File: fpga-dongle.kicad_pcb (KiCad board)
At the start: 2 copper layers, 85.8 x 137 mm, 82 parts, among them P1 right, P2 left, P3 CONN_01X20, U1 W25Q16BVSSIG(SOIC-8_208mil), U2 SY8009AAAC(SOT23-5), U3 SY8009AAAC(SOT23-5), U4 ICE40HX1K-VQ100(VQFP100), U5 AS4C16M16S

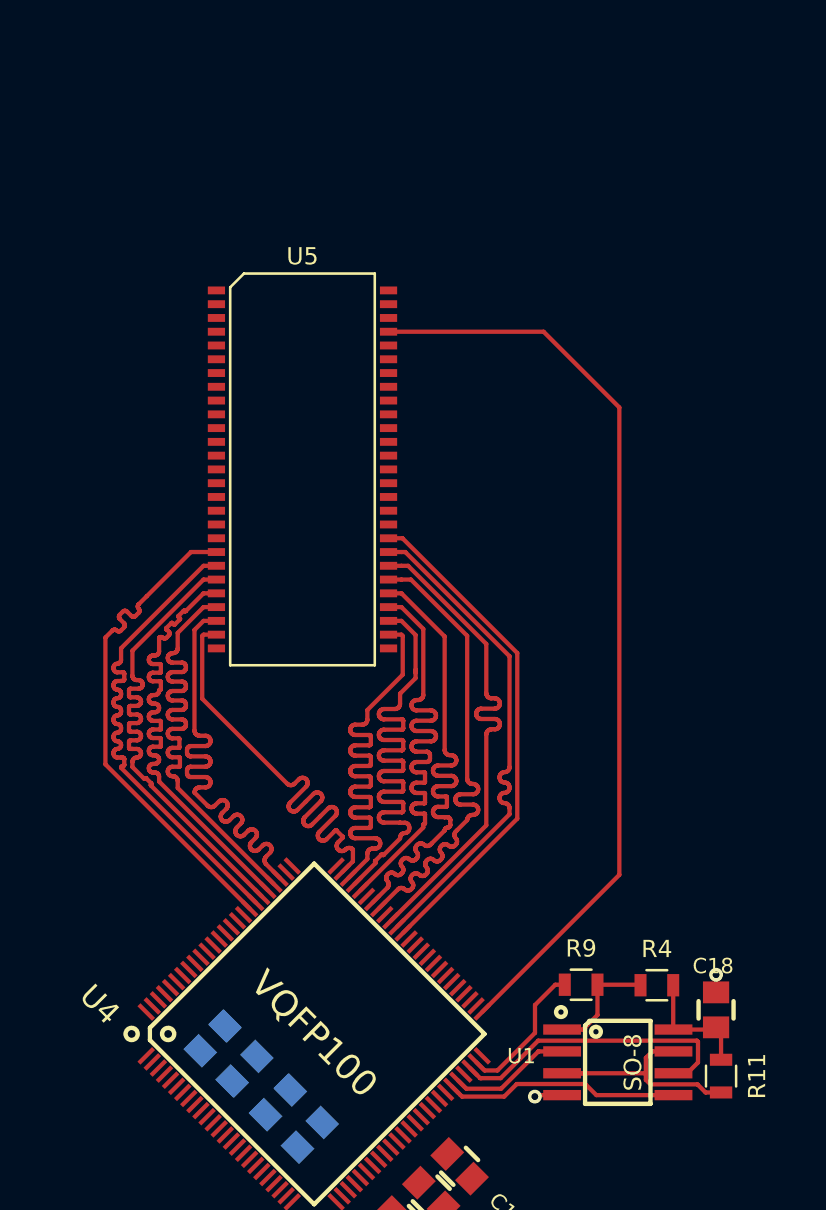
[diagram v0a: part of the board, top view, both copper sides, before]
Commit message: First 144LQFP version. To be revised
Signed-off-by: Martin Ribelotta <martinribelotta@gmail.com>
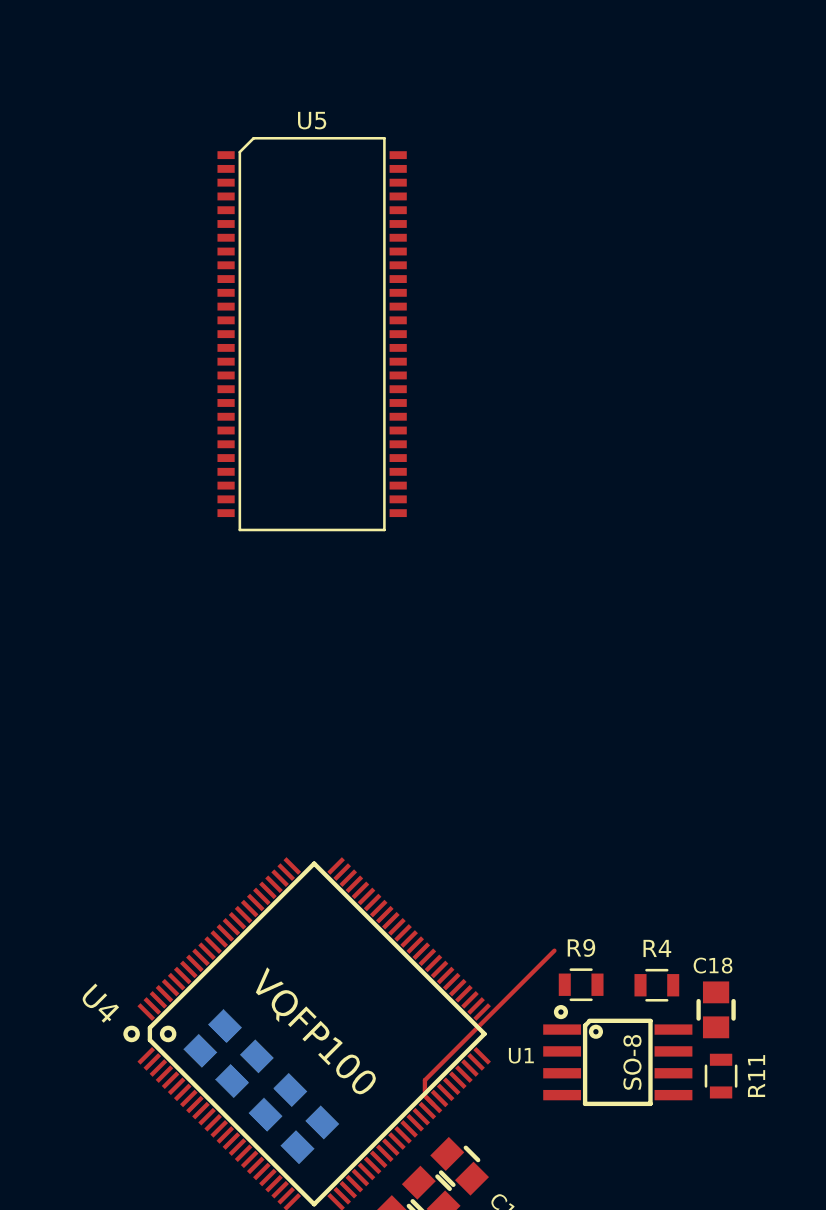
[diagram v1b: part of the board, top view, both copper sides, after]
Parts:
- moved U5 7.88 mm to (61.3, 69.4)
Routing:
- net /RAM_D14: track 53.7 -> 0.00 mm
- net /RAM_A6: track 33.4 -> 0.00 mm
- net /RAM_A2: track 29.3 -> 0.00 mm
- net /RAM_A15: track 29.3 -> 0.00 mm
- net /RAM_A4: track 29.3 -> 0.00 mm
- net /RAM_A8: track 29.3 -> 0.00 mm
- net /RAM_A7: track 29.3 -> 0.00 mm
- net /RAM_A3: track 29.3 -> 0.00 mm
- net /RAM_A12: track 29.3 -> 0.00 mm
- net /RAM_A9: track 29.3 -> 0.00 mm
- net /RAM_A1: track 29.3 -> 0.00 mm
- net /RAM_A10: track 29.3 -> 0.00 mm
- net /RAM_A11: track 29.3 -> 0.00 mm
- net /RAM_A13: track 29.3 -> 0.00 mm
- net /RAM_A5: track 29.2 -> 0.00 mm
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
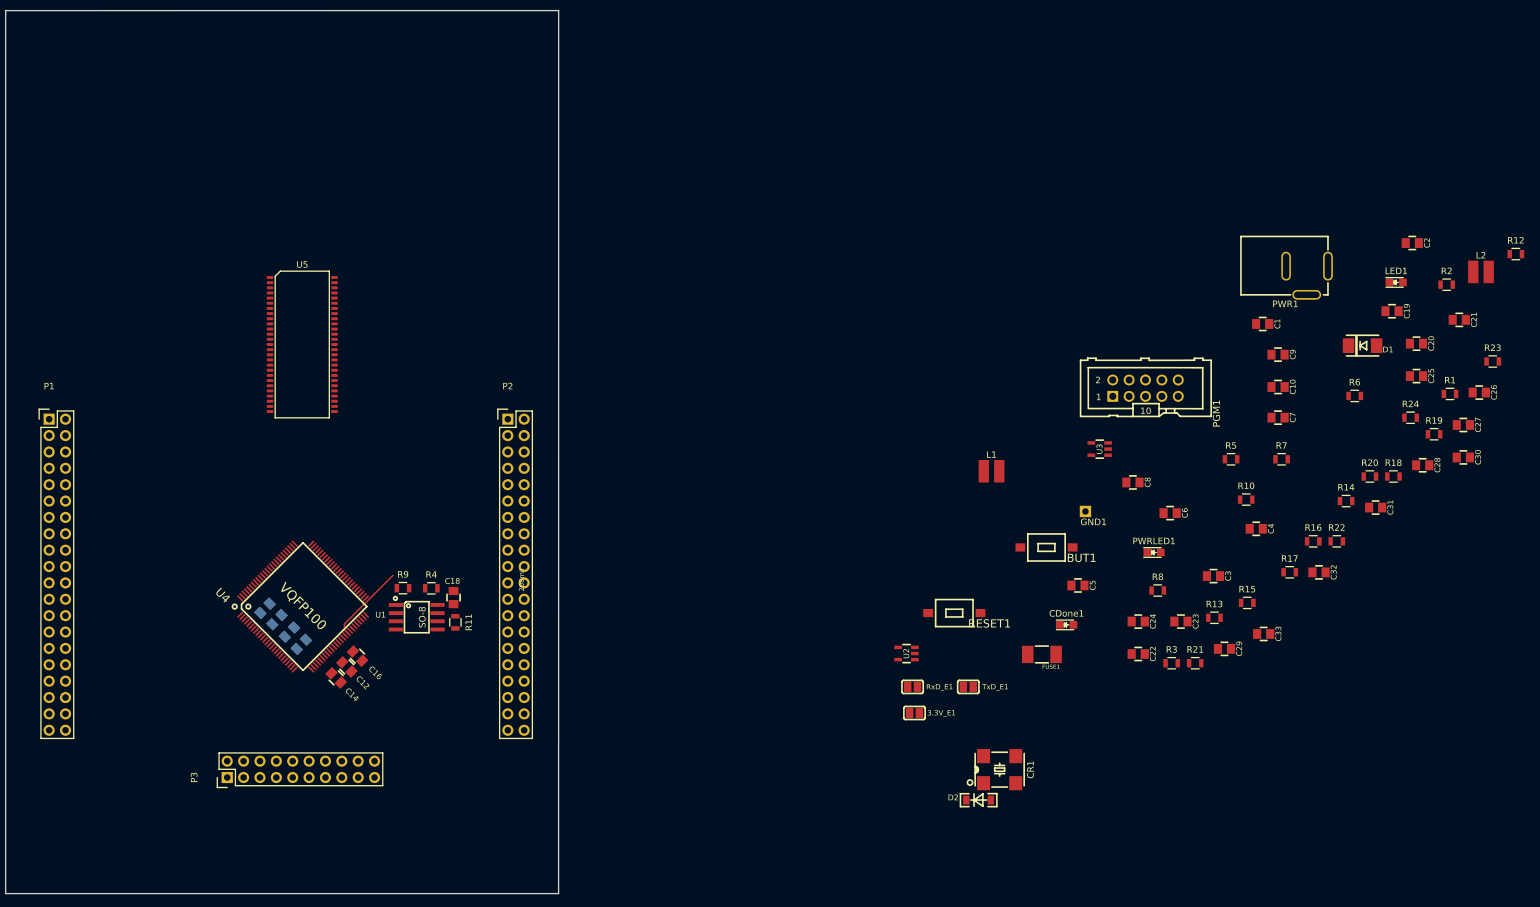
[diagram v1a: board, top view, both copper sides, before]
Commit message: First component assign and preeliminar place
Signed-off-by: Martin Ribelotta <martinribelotta@gmail.com>
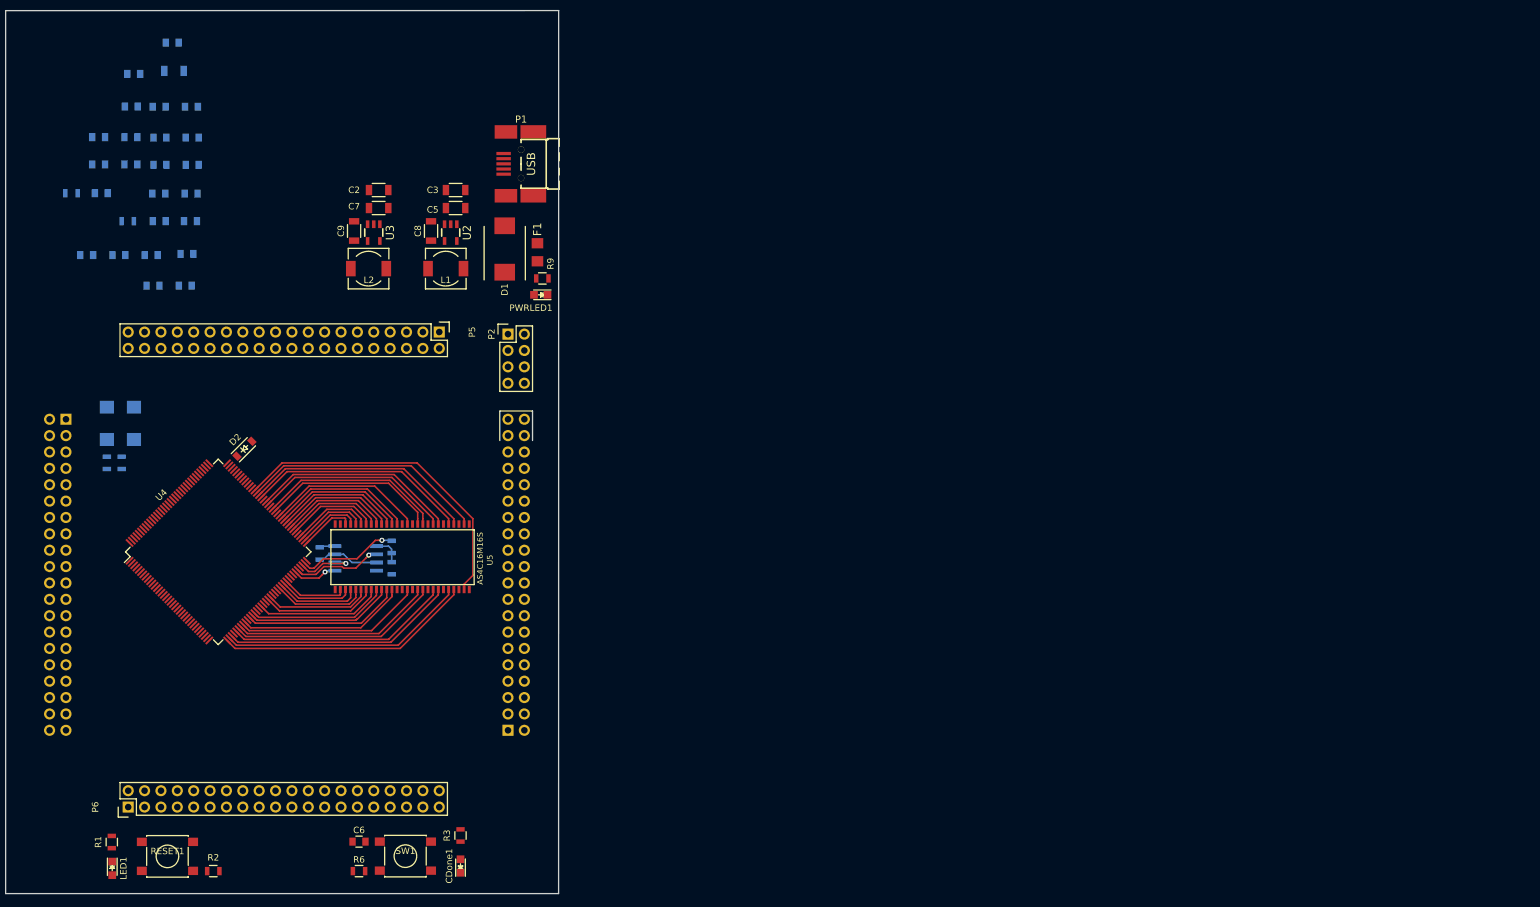
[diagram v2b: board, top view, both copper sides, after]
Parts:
- removed 3.3V_E1, RxD_E1, TxD_E1: Opened, OLIMEX:SJ
- removed BUT1: T1107A(6x3,8x2,5MM), OLIMEX:T1107A(6x3,8x2,5MM)
- removed C33: 100n, OLIMEX:C_0805_5MIL_DWS
- removed FUSE1: NA(5025), OLIMEX:FUSE-5025
- removed GND1: TESTPAD, OLIMEX:TEST_PAD40x70_SQUARE
- removed PGM1: BH10S, OLIMEX:UEXT_ML10
- removed PWR1: PWRJ-2mm(YDJ-1136), OLIMEX:PWRJ-2mm(YDJ-1136)
- removed R13: 22R, Resistors_SMD:R_0805
- removed R14, R15: 2.2k, Resistors_SMD:R_0805
- removed R16: 10k, Resistors_SMD:R_0805
- removed R17, R18, R19, R20, R21, R22, R23, R24: 0, Resistors_SMD:R_0805
- added F1: 1A, OLIMEX_Devices-FP:FUSE-1206, F.Cu at (97.8, 55.1)
- added P4: left, Pin_Headers:Pin_Header_Straight_2x20, B.Cu at (93.2, 129.3)
- added P5: CONN_01X40, Pin_Headers:Pin_Header_Straight_2x20, F.Cu at (82.6, 67.5)
- added P6: CONN_01X40, Pin_Headers:Pin_Header_Straight_2x20, F.Cu at (34.3, 141.2)
- added SW1: T1107A(6x3,8x2,5MM), Buttons_Switches_SMD:SW_SPST_PTS645, F.Cu at (77.3, 148.8)
- C1, C10: value 22uF/6.3V/0603 -> 100nF; footprint OLIMEX:C_0805_5MIL_DWS -> Capacitors_SMD:C_0805; moved to B.Cu
- C11: value 100nF -> 10uF; footprint OLIMEX:C_0805_5MIL_DWS -> Capacitors_SMD:C_1206
- C12, C14, C16, C18, C20, C21, C22, C23, C24, C25, C4: footprint OLIMEX:C_0805_5MIL_DWS -> Capacitors_SMD:C_0805; moved to B.Cu
- C13, C15, C17: footprint OLIMEX:C_0805_5MIL_DWS -> Capacitors_SMD:C_0805
- C19: value NA(100nF) -> 100nF; footprint OLIMEX:C_0805_5MIL_DWS -> Capacitors_SMD:C_0805; moved to B.Cu
- C2, C5: footprint OLIMEX:C_0805_5MIL_DWS -> Capacitors_SMD:C_1206
- C26: value 100p -> 100nF; footprint OLIMEX:C_0805_5MIL_DWS -> Capacitors_SMD:C_0805; moved to B.Cu
- C27, C28, C29, C30, C31, C32: value 100n -> 100nF; footprint OLIMEX:C_0805_5MIL_DWS -> Capacitors_SMD:C_0805; moved to B.Cu
- C3: value 100nF -> 22uF/6.3V/0603; footprint OLIMEX:C_0805_5MIL_DWS -> Capacitors_SMD:C_1206
- C6: value 47uF/6.3V/0805 -> NA(100nF); footprint OLIMEX:C_0805_5MIL_DWS -> Capacitors_SMD:C_0805
- C7: value 22uF/6.3V/0603 -> 47uF/6.3V/0805; footprint OLIMEX:C_0805_5MIL_DWS -> Capacitors_SMD:C_1206
- C8, C9: value 22uF/6.3V/0603 -> 10uF/6.3V/0603; footprint OLIMEX:C_0805_5MIL_DWS -> Capacitors_SMD:C_1206
- CR1: value Oscillator-100MHZ_TXC-7W -> Oscillator-50MHZ_TXC-7W; footprint OLIMEX:Oscillator_7.0x5.0mm -> OLIMEX_Crystal-FP:Oscillator_7.0x5.0mm; moved to B.Cu
- D1: footprint OLIMEX:DO214AA -> Diodes_SMD:DO-214AB
- D2: footprint OLIMEX:SOD-123_1C-2A_KA -> Diodes_SMD:SOD-123
- L1, L2: value 2.2uH/1.5A/DCR<0.1R/CD32 -> 2.2uH; footprint OLIMEX:CD32 -> Choke_SMD:Choke_SMD_6.3x6.3_H3
- P1: value right -> USB_PWR; footprint Pin_Headers:Pin_Header_Straight_2x20 -> OLIMEX_Connectors-FP:USB_Mini-B-NOSILK
- P2: value left -> PGM; footprint Pin_Headers:Pin_Header_Straight_2x20 -> Pin_Headers:Pin_Header_Straight_2x04
- P3: value CONN_01X20 -> right; footprint Pin_Headers:Pin_Header_Straight_2x10 -> Pin_Headers:Pin_Header_Straight_2x20; moved to B.Cu
- R1: value 10k -> 2.2k
- R10: value NA(22R) -> 22R; moved to B.Cu
- R11, R4: value 10k -> 22R; moved to B.Cu
- R12: value 22R -> 100R; moved to B.Cu
- R2: value 2.2k -> 10k
- R3, R9: value 22R -> 2.2k
- R5, R8: value 4.99k/1% -> 10k; moved to B.Cu
- R6: value 1.1k/1% -> 10k
- R7: value 4.99k/1% -> 22R; moved to B.Cu
- RESET1: footprint OLIMEX:T1107A(6x3,8x2,5MM) -> Buttons_Switches_SMD:SW_SPST_PTS645
- U1: footprint OLIMEX:SO-8_208mil -> OLIMEX_IC-FP:SOIC-8_208mil; moved to B.Cu
- U2: value SY8009AAAC(SOT23-5) -> sc189(Z) 3.3v; footprint OLIMEX:SOT-23-5 -> OLIMEX_Regulators-FP:SOT-23-5
- U3: value SY8009AAAC(SOT23-5) -> sc189(C) 1.2v; footprint OLIMEX:SOT-23-5 -> OLIMEX_Regulators-FP:SOT-23-5
- U4: value ICE40HX1K-VQ100(VQFP100) -> iCE40-HX4K-TQ144; footprint OLIMEX:VQFP100_Pitch-0.5mm_Dimensions-16.00x16.00x1.20mm -> Housings_QFP:LQFP-144_20x20mm_Pitch0.5mm
- U5: footprint OLIMEX:SOIC-54 -> mribelotta:TSOP_II_54
- moved R12 224.3 mm to (25.5, 46.0), turned to 180 degrees
- moved LED1 219.0 mm to (31.8, 150.7), turned to 270 degrees
- moved R1 219.0 mm to (31.8, 146.6), turned to 90 degrees
- moved C30 216.6 mm to (29.7, 41.5), turned to 180 degrees
- moved C26 213.8 mm to (34.8, 32.5), turned to 180 degrees
- moved R2 211.9 mm to (47.5, 151.1)
- moved C28 211.6 mm to (29.7, 37.3), turned to 180 degrees
- moved C21 203.6 mm to (39.2, 37.3), turned to 180 degrees
- moved C27 199.8 mm to (43.4, 55.4), turned to 180 degrees
- moved C25 197.7 mm to (39.2, 41.6), turned to 180 degrees
- moved C20 191.2 mm to (43.2, 60.3), turned to 180 degrees
- moved C31 190.1 mm to (44.1, 46.0), turned to 180 degrees
- moved C32 189.3 mm to (39.0, 46.0), turned to 180 degrees
- moved C19 188.1 mm to (44.2, 37.3), turned to 180 degrees
- moved C29 185.6 mm to (34.7, 41.5), turned to 180 degrees
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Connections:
- C1 pad 2: +5V -> +3V3
- C10 pad 1: GND -> /GNDPLL
- C10 pad 2: +1V2 -> /VCCPLL
- C11 pad 1: GND -> /GNDPLL
- C11 pad 2: +1V2 -> /VCCPLL
- C12 pad 1: GND -> +1V2
- C12 pad 2: +1V2 -> GND
- C13 pad 1: GND -> +1V2
- C13 pad 2: +3V3 -> GND
- C14 pad 1: GND -> +1V2
- C14 pad 2: +3V3 -> GND
- C15 pad 1: GND -> +1V2
- C15 pad 2: +3V3 -> GND
- C16 pad 1: GND -> +3V3
- C16 pad 2: +3V3 -> GND
- C17 pad 1: GND -> +3V3
- C17 pad 2: +3V3 -> GND
- C18 pad 1: GND -> +3V3
- C18 pad 2: +3V3 -> GND
- C19 pad 1: GND -> +3V3
- C19 pad 2: /BUT1 -> GND
- C20 pad 1: GND -> +3V3
- C20 pad 2: +3V3 -> GND
- C21 pad 1: GND -> +3V3
- C21 pad 2: +3V3 -> GND
- C22 pad 1: GND -> +3V3
- C22 pad 2: +3V3 -> GND
- C23 pad 1: GND -> +3V3
- C23 pad 2: +1V2 -> GND
- C24 pad 1: GND -> +3V3
- C24 pad 2: +3V3 -> GND
- C25 pad 1: GND -> +3V3
- C25 pad 2: +1V2 -> GND
- C3 pad 2: +3V3 -> +5V
- C6 pad 2: +5V -> /BUT1
- C7 pad 2: +3V3 -> +5V
- C8 pad 2: +1V2 -> +3V3
- C9 pad 2: +3V3 -> +1V2
- D2 pad 2: +3V3 -> +1V2
- L1 pad 1: +3V3 -> Net-(L1-Pad1)
- L1 pad 2: Net-(L1-Pad2) -> +3V3
- L2 pad 1: +1V2 -> Net-(L2-Pad1)
- L2 pad 2: Net-(L2-Pad2) -> +1V2
- P1 pad 1: +3V3 -> Net-(F1-Pad1)
- P1 pad 11: GND -> (no net)
- P1 pad 3: GND -> (no net)
- P1 pad 7: GND -> (no net)
- P2 pad 1: +3V3 -> /iCE40-CDONE
- P2 pad 2: (no net) -> /iCE40-CRESET
- P2 pad 3: (no net) -> /iCE40-SDI
- P2 pad 4: GND -> /iCE40-SDO
- P2 pad 5: (no net) -> /iCE40-SCK
- P2 pad 6: (no net) -> /iCE40-SS_B
- P2 pad 8: GNDA -> GND
- P3 pad 1: /PIO3_1A -> +3V3
- P3 pad 10: /PIO3_6B -> (no net)
- P3 pad 11: /SYSCLK -> GND
- P3 pad 12: /PIO3_7B -> (no net)
- P3 pad 13: /PIO3_8A -> GND
- P3 pad 14: /PIO3_8B -> (no net)
- P3 pad 15: /PIO3_10A -> (no net)
- P3 pad 16: /PIO3_10B -> (no net)
- P3 pad 17: /PIO3_12A -> GND
- P3 pad 18: /PIO3_12B -> /SPI_MISO
- P3 pad 19: /PIO2_1 -> GND
- P3 pad 2: /PIO3_1B -> (no net)
- P3 pad 20: GND -> (no net)
- P3 pad 3: /PIO3_2A -> GND
- P3 pad 4: /PIO3_2B -> (no net)
- P3 pad 5: /PIO3_3A -> GND
- P3 pad 6: /PIO3_3B -> (no net)
- P3 pad 7: /PIO3_5A -> GND
- P3 pad 8: /PIO3_5B -> (no net)
- P3 pad 9: /PIO3_6A -> (no net)
- R1 pad 1: /iCE40-CRESET -> Net-(LED1-Pad1)
- R1 pad 2: +3V3 -> GND
- R10 pad 1: /iCE40-SDI -> /SYSCLK
- R10 pad 2: /iCE40-SDO -> Net-(CR1-Pad3)
- R11 pad 1: +3V3 -> (no net)
- R11 pad 2: Net-(R11-Pad2) -> Net-(CR1-Pad3)
- R12 pad 1: /SYSCLK -> +1V2
- R12 pad 2: Net-(CR1-Pad3) -> /VCCPLL
- R2 pad 1: /iCE40-CDONE -> /iCE40-CRESET
- R3 pad 1: Net-(CDone1-Pad1) -> /iCE40-CDONE
- R3 pad 2: GND -> +3V3
- R4 pad 1: Net-(R4-Pad1) -> Net-(CDone1-Pad1)
- R4 pad 2: +3V3 -> GND
- R5 pad 1: +3V3 -> Net-(R5-Pad1)
- R5 pad 2: Net-(R5-Pad2) -> +3V3
- R6 pad 1: GND -> /BUT1
- R6 pad 2: Net-(R5-Pad2) -> +3V3
- R7 pad 1: +1V2 -> /iCE40-SS_B
- R7 pad 2: Net-(R7-Pad2) -> Net-(R5-Pad1)
- R8 pad 1: GND -> +3V3
- R8 pad 2: Net-(R7-Pad2) -> Net-(R8-Pad2)
- R9 pad 1: /iCE40-SS_B -> +5V
- R9 pad 2: Net-(R4-Pad1) -> Net-(PWRLED1-Pad2)
- RESET1 pad 1: /iCE40-CRESET -> GND
- RESET1 pad 2: GND -> /iCE40-CRESET
- U1 pad 1: Net-(R4-Pad1) -> Net-(R5-Pad1)
- U1 pad 3: Net-(R11-Pad2) -> Net-(R8-Pad2)
- U1 pad 7: Net-(R11-Pad2) -> Net-(R8-Pad2)
- U2 pad 3: Net-(L1-Pad2) -> +5V
- U2 pad 4: +5V -> +3V3
- U2 pad 5: Net-(R5-Pad2) -> Net-(L1-Pad1)
- U3 pad 3: Net-(L2-Pad2) -> +5V
- U3 pad 4: +5V -> +1V2
- U3 pad 5: Net-(R7-Pad2) -> Net-(L2-Pad1)
- U4 pad 1: /PIO3_1A -> /FPGA_IO_BANK2_0
- U4 pad 10: /PIO3_5B -> /FPGA_IO_BANK2_7
- U4 pad 100: /RAM_D0 -> +3V3
- U4 pad 11: +1V2 -> /FPGA_IO_BANK2_8
- U4 pad 12: /PIO3_6A -> /FPGA_IO_BANK2_9
- U4 pad 13: /PIO3_6B -> GND
- U4 pad 14: +3V3 -> GND
- U4 pad 15: /SYSCLK -> /FPGA_IO_BANK2_10
- U4 pad 16: /PIO3_7B -> /FPGA_IO_BANK2_11
- U4 pad 17: GND -> /FPGA_IO_BANK2_12
- U4 pad 18: /PIO3_8A -> /FPGA_IO_BANK2_13
- U4 pad 19: /PIO3_8B -> /FPGA_IO_BANK2_14
- U4 pad 2: /PIO3_1B -> /FPGA_IO_BANK2_1
- U4 pad 20: /PIO3_10A -> /FPGA_IO_BANK2_15
- U4 pad 21: /PIO3_10B -> /FPGA_IO_BANK2_16
- U4 pad 22: +3V3 -> /FPGA_IO_BANK2_17
- U4 pad 23: GND -> /FPGA_IO_BANK2_18
- U4 pad 24: /PIO3_12A -> /FPGA_IO_BANK2_19
- U4 pad 25: /PIO3_12B -> /FPGA_IO_BANK2_20
- U4 pad 26: /PIO2_1 -> /FPGA_IO_BANK2_21
- U4 pad 27: /PIO2_2/I2C_SDA -> +1V2
- U4 pad 28: /PIO2_3/I2C_SCL -> /FPGA_IO_BANK2_22
- U4 pad 29: /PIO2_4/SPI_CS -> /FPGA_IO_BANK2_23
- U4 pad 3: /PIO3_2A -> /FPGA_IO_BANK2_2
- U4 pad 30: /PIO2_5/SPI_MOSI -> +3V3
- U4 pad 31: +3V3 -> /FPGA_IO_BANK2_24
- U4 pad 32: GND -> /FPGA_IO_BANK2_25
- U4 pad 33: /PIO2_6/SPI_MISO -> /FPGA_IO_BANK2_26
- U4 pad 34: /PIO2_7/SPI_CLK -> /FPGA_IO_BANK2_27
- U4 pad 35: +1V2 -> (no net)
- U4 pad 36: /PIO2_8/RxD -> (no net)
- U4 pad 37: /PIO2_9/TxD -> /RAM_D14
- U4 pad 38: +3V3 -> /RAM_D13
- U4 pad 39: GND -> /RAM_D12
- U4 pad 4: /PIO3_2B -> /FPGA_IO_BANK2_3
- U4 pad 40: /LED1 -> +1V2
- U4 pad 41: /BUT1 -> /RAM_D11
- U4 pad 42: /RAM_D15 -> /RAM_D10
- U4 pad 43: /iCE40-CDONE -> /RAM_D9
- U4 pad 44: /iCE40-CRESET -> /RAM_D8
- U4 pad 45: /iCE40-SDO -> /RAM_DQMH
- U4 pad 46: /iCE40-SDI -> +3V3
- U4 pad 47: GND -> /RAM_CLK
- U4 pad 48: /iCE40-SCK -> /RAM_CKE
- U4 pad 49: /iCE40-SS_B -> /RAM_A13
- U4 pad 50: +3V3 -> (no net)
- U4 pad 51: /RAM_D14 -> (no net)
- U4 pad 52: /RAM_D13 -> /RAM_A12
- U4 pad 53: /RAM_D12 -> /GNDPLL
- U4 pad 54: /RAM_D11 -> /VCCPLL
- U4 pad 55: GND -> /RAM_A10
- U4 pad 56: /RAM_D10 -> /RAM_A9
- U4 pad 57: /RAM_D9 -> +3V3
- U4 pad 58: +3V3 -> (no net)
- U4 pad 59: /RAM_D8 -> GND
- U4 pad 60: /RAM_DQMH -> /RAM_A8
- U4 pad 61: +1V2 -> /RAM_A7
- U4 pad 62: /RAM_CLK -> /RAM_A6
- U4 pad 63: /RAM_CKE -> /RAM_A5
- U4 pad 64: /RAM_A13 -> /RAM_A4
- U4 pad 65: /RAM_A12 -> /iCE40-CDONE
- U4 pad 66: /RAM_A10 -> /iCE40-CRESET
- U4 pad 67: +3V3 -> /iCE40-SDO
- U4 pad 68: /RAM_A9 -> /iCE40-SDI
- U4 pad 69: /RAM_A8 -> GND
- U4 pad 7: /PIO3_3A -> /FPGA_IO_BANK2_4
- U4 pad 70: GND -> /iCE40-SCK
- U4 pad 71: /RAM_A7 -> /iCE40-SS_B
- U4 pad 72: /RAM_A6 -> +3V3
- U4 pad 73: /RAM_A5 -> /RAM_A3
- U4 pad 74: /RAM_A4 -> /RAM_A2
- U4 pad 75: Net-(D2-Pad1) -> /RAM_A1
- U4 pad 76: (no net) -> /RAM_A11
- U4 pad 77: +1V2 -> (no net)
- U4 pad 78: /RAM_A3 -> /RAM_A15
- U4 pad 79: /RAM_A2 -> /RAM_A14
- U4 pad 8: /PIO3_3B -> /FPGA_IO_BANK2_5
- U4 pad 80: /RAM_A1 -> /RAM_CS
- U4 pad 81: /RAM_A11 -> /RAM_RAS
- U4 pad 82: /RAM_A15 -> /RAM_CAS
- U4 pad 83: /RAM_A14 -> /RAM_RDnWR
- U4 pad 84: GND -> /RAM_DQML
- U4 pad 85: /RAM_CS -> /RAM_D7
- U4 pad 86: /RAM_RAS -> GND
- U4 pad 87: /RAM_CAS -> /RAM_D6
- U4 pad 88: +3V3 -> /RAM_D5
- U4 pad 89: /RAM_RDnWR -> +3V3
- U4 pad 9: /PIO3_5A -> /FPGA_IO_BANK2_6
- U4 pad 90: /RAM_DQML -> /RAM_D4
- U4 pad 91: /RAM_D7 -> /RAM_D3
- U4 pad 92: +3V3 -> +1V2
- U4 pad 93: /RAM_D6 -> /RAM_D2
- U4 pad 94: /RAM_D5 -> /RAM_D1
- U4 pad 95: /RAM_D4 -> /RAM_D0
- U4 pad 96: /RAM_D3 -> /RAM_D15
- U4 pad 97: /RAM_D2 -> /I2C_SDA
- U4 pad 98: GND -> /I2C_SCL
- U4 pad 99: /RAM_D1 -> /SPI_CS
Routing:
- net /RAM_D14: track 0.00 -> 40.0 mm
- net /RAM_D15: track 12.3 -> 50.8 mm
- net /RAM_D13: track 0.00 -> 38.5 mm
- net /RAM_D0: track 0.00 -> 38.1 mm
- net /RAM_D12: track 0.00 -> 36.3 mm
- net /RAM_D1: track 0.00 -> 36.0 mm
- net /RAM_D11: track 0.00 -> 34.8 mm
- net /RAM_D2: track 0.00 -> 34.6 mm
- net /RAM_D10: track 0.00 -> 32.6 mm
- net /RAM_D3: track 0.00 -> 32.2 mm
- net /RAM_D9: track 0.00 -> 31.2 mm
- net /RAM_D4: track 0.00 -> 30.8 mm
- net /RAM_D8: track 0.00 -> 29.0 mm
- net /RAM_D5: track 0.00 -> 28.9 mm
- net /RAM_D6: track 0.00 -> 27.6 mm
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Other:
- outline, holes or cut-outs redrawn
